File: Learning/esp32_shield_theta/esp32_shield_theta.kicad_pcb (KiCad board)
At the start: 2 copper layers, 39.9 x 73.2 mm, 16 parts, among them J1 Conn_01x06, J2 DE9_Plug, U1 ESP32-DEVKIT-V1, U2 LM358

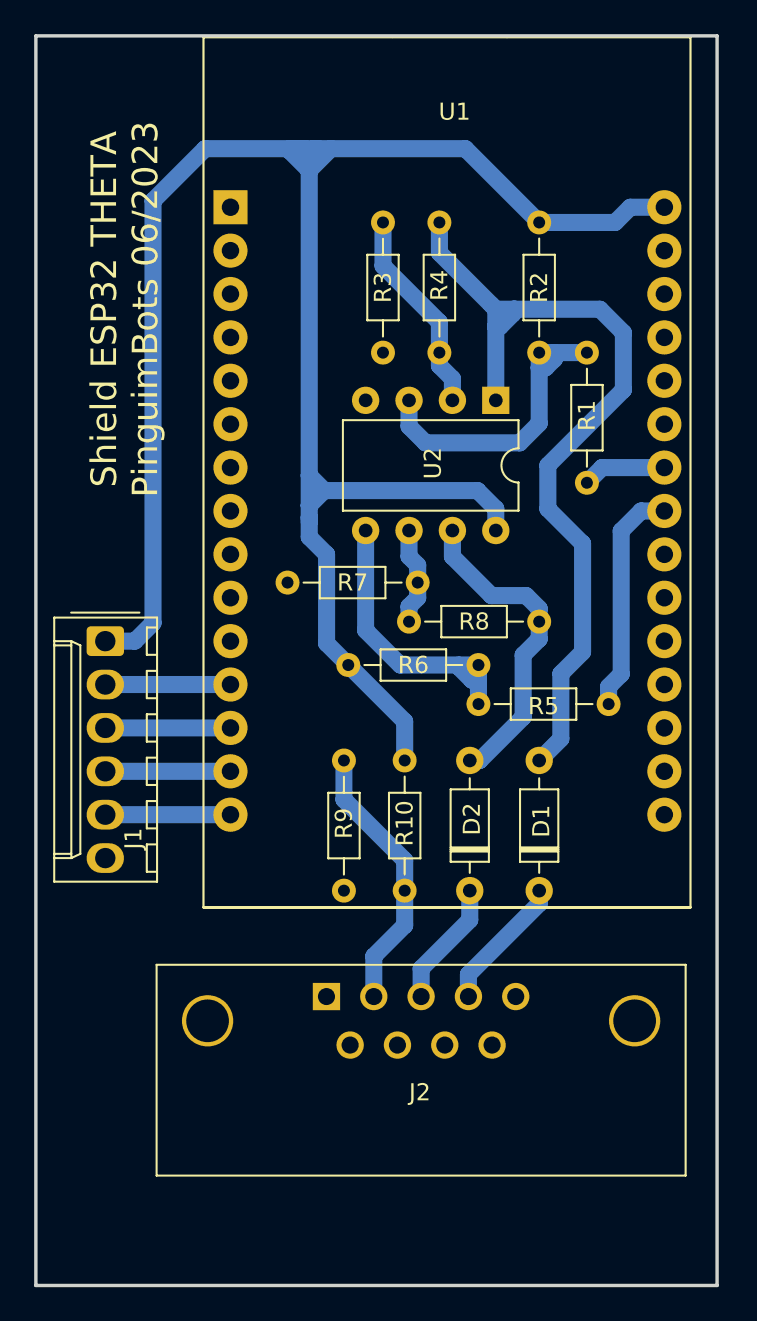
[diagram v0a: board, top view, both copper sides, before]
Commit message: Update on esp32 theta
change to a up to date version
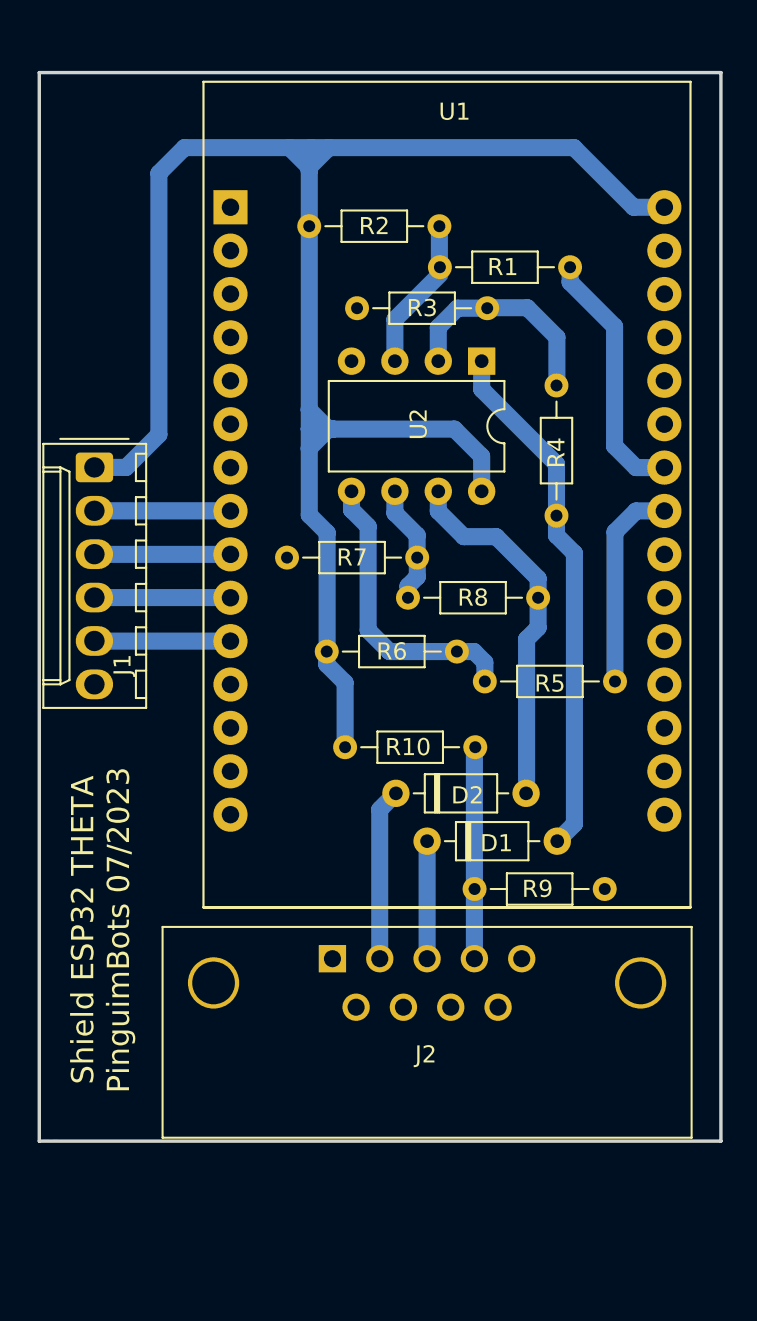
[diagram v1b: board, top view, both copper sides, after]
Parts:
- J1: value Conn_01x06 -> Mini kk
- J2: value DE9_Plug -> DB9
- moved R9 15.3 mm to (144.3, 94.9), turned to 180 degrees
- moved R2 13.5 mm to (127.0, 56.1), turned to 0 degrees
- moved R1 12.7 mm to (142.3, 58.5), turned to 180 degrees
- moved J1 10.2 mm to (114.4, 70.2)
- moved D1 7.17 mm to (133.9, 92.1), turned to 0 degrees
- moved D2 7.15 mm to (132.1, 89.3), turned to 0 degrees
- moved R4 7.12 mm to (141.5, 65.4), turned to -90 degrees
- moved R10 3.57 mm to (129.1, 86.6), turned to 0 degrees
- moved R3 3.01 mm to (129.8, 60.9), turned to 0 degrees
- moved U2 2.44 mm to (137.1, 64.0)
- moved J2 2.24 mm to (128.4, 99.0)
- moved R6 1.49 mm to (128.0, 81.0)
- moved R7 1.46 mm to (125.7, 75.5)
- moved R8 1.40 mm to (132.8, 77.8)
- moved R5 1.38 mm to (144.9, 82.8)
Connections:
- J1 pad 2: BRightHall -> ARightHall
- J1 pad 3: ARightHall -> BRightHall
- J1 pad 4: BLeftHall -> ALeftHall
- J1 pad 5: ALeftHall -> BLeftHall
- J2 pad 1: GND -> unconnected-(J2-Pad1)
- J2 pad 2: 2.5V -> YChannel
- J2 pad 3: YChannel -> XChannel
- J2 pad 4: XChannel -> 2.5V
- J2 pad 5: unconnected-(J2-Pad5) -> GND
- U1 pad 10: unconnected-(U1-D19-Pad10) -> ALeftHall
- U1 pad 11: unconnected-(U1-D21-Pad11) -> BLeftHall
- U1 pad 12: BRightHall -> unconnected-(U1-RX0-Pad12)
- U1 pad 13: ARightHall -> unconnected-(U1-TX0-Pad13)
- U1 pad 14: BLeftHall -> unconnected-(U1-D22-Pad14)
- U1 pad 15: ALeftHall -> unconnected-(U1-D23-Pad15)
- U1 pad 8: unconnected-(U1-D5-Pad8) -> ARightHall
- U1 pad 9: unconnected-(U1-D18-Pad9) -> BRightHall
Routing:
- net Net-(D1-A): track 50.3 -> 30.8 mm
- net +5V: track 119.6 -> 107.1 mm
- net DAC1: track 4.54 -> 15.0 mm
- net Net-(U2A-+): track 18.4 -> 8.58 mm
- net 2.5V: track 16.0 -> 12.3 mm
- net Net-(D2-A): track 18.8 -> 21.5 mm
- net YChannel: track 7.38 -> 10.1 mm
- net DAC2: track 13.5 -> 12.1 mm
- net Net-(U2B--): track 5.75 -> 7.00 mm
- net XChannel: track 7.92 -> 6.88 mm
- net Net-(U2A--): track 12.1 -> 12.8 mm
- net BRightHall: track 7.33 -> 7.97 mm
- net BLeftHall: track 7.33 -> 7.97 mm
- net ARightHall: track 7.33 -> 7.97 mm
- net ALeftHall: track 7.33 -> 7.97 mm
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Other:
- board size 39.9 x 73.2 mm -> 39.9 x 62.6 mm
- board text added: "Shield ESP32 THETA PinguimBots 07/2023"
- board text removed: "Shield ESP32 THETA PinguimBots 06/2023"
